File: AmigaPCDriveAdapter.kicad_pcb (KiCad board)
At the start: 2 copper layers, 99.1 x 30.5 mm, 19 parts, among them P1 CONN_01X04, P2 CONN_01X04, U1 74LS38

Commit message: Version Kicad 5 V2.0
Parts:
- removed LOGO: Symbol_OSHW-Logo_SilkScreen, Symbols:Symbol_OSHW-Logo_SilkScreen
- added OSHW: OSHW-Logo_5.7x6mm_SilkScreen, Symbol:OSHW-Logo_5.7x6mm_SilkScreen, F.Cu at (163.5, 118.5)
- C1, C4: footprint Capacitors_SMD:C_1206_HandSoldering -> Capacitor_Tantalum_SMD:CP_EIA-3216-12_Kemet-S
- C2: footprint Capacitors_SMD:C_1206_HandSoldering -> Capacitor_SMD:C_1206_3216Metric_Pad1.42x1.75mm_HandSolder
- C3: footprint Capacitors_SMD:C_1206_HandSoldering -> Capacitor_SMD:C_1206_3216Metric_Pad1.42x1.75mm_HandSolder; moved to B.Cu
- D1: footprint LEDs:LED_1206 -> LED_SMD:LED_1206_3216Metric_Pad1.42x1.75mm_HandSolder
- P1: footprint Pin_Headers:Pin_Header_Straight_1x04 -> Connector_PinHeader_2.54mm:PinHeader_1x04_P2.54mm_Vertical
- P2: footprint Pin_Headers:Pin_Header_Angled_1x04 -> Connector_PinHeader_2.54mm:PinHeader_1x04_P2.54mm_Horizontal
- R1, R2, R6, R8: footprint Resistors_SMD:R_1206_HandSoldering -> Resistor_SMD:R_1206_3216Metric_Pad1.42x1.75mm_HandSolder
- R3, R4, R5, R7: footprint Resistors_SMD:R_1206_HandSoldering -> Resistor_SMD:R_1206_3216Metric_Pad1.42x1.75mm_HandSolder; moved to B.Cu
- TO_FLOPPY1: footprint Socket_Strips:Socket_Strip_Straight_2x17 -> Connector_PinSocket_2.54mm:PinSocket_2x17_P2.54mm_Vertical
- U1: footprint Housings_DIP:DIP-14_W7.62mm -> Package_DIP:DIP-14_W7.62mm
- moved C3 58.1 mm to (164.2, 113.0)
- moved R7 51.2 mm to (145.6, 118.1), turned to 180 degrees
- moved R5 46.3 mm to (155.8, 118.1)
- moved C2 34.1 mm to (178.7, 103.5)
- moved R6 31.0 mm to (221.2, 111.1)
- moved R1 30.5 mm to (185.4, 104.8)
- moved R2 18.3 mm to (203.2, 111.1)
- moved R8 11.7 mm to (173.8, 109.2), turned to 0 degrees
- moved C4 10.9 mm to (164.5, 106.0), turned to 180 degrees
- moved U1 10.2 mm to (157.5, 114.3)
- moved R4 6.18 mm to (211.0, 109.9)
- moved TO_AMIGA1 5.08 mm to (172.7, 119.4)
- moved TO_FLOPPY1 2.54 mm to (180.3, 99.1), turned to 270 degrees
- moved C1 2.16 mm to (177.2, 98.4)
- moved R3 1.95 mm to (211.2, 104.8)
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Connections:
- TO_FLOPPY1 pad 2: (no net) -> Net-(TO_FLOPPY1-Pad2)
- U1 pad 10: (no net) -> Net-(U1-Pad10)
- U1 pad 11: (no net) -> Net-(U1-Pad11)
- U1 pad 12: (no net) -> Net-(U1-Pad12)
- U1 pad 13: (no net) -> Net-(U1-Pad13)
- U1 pad 8: (no net) -> Net-(U1-Pad8)
- U1 pad 9: (no net) -> Net-(U1-Pad9)
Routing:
- net +5V: track 161.3 -> 111.4 mm, vias 2 -> 1
- net Net-(R5-Pad1): track 47.0 -> 10.3 mm
- net ~REDWC: track 73.5 -> 108.2 mm, vias 2 -> 0
- net +12V: track 83.4 -> 50.0 mm
- net ~RDATA: track 52.5 -> 23.7 mm, vias 1 -> 0
- net ~INDEX: track 51.4 -> 32.7 mm, vias 1 -> 0
- net GND: track 184.9 -> 175.1 mm, vias 1 -> 0
- net ~MOTEA: track 44.2 -> 53.7 mm
- net ~TRK00: track 33.0 -> 25.0 mm
- net Net-(TO_AMIGA1-Pad4): track 19.0 -> 23.7 mm
- net Net-(TO_AMIGA1-Pad24): track 19.0 -> 23.7 mm
- net Net-(TO_AMIGA1-Pad18): track 19.0 -> 23.7 mm
- net Net-(TO_AMIGA1-Pad16): track 19.0 -> 23.7 mm
- net Net-(TO_AMIGA1-Pad22): track 19.0 -> 23.7 mm
- net Net-(TO_AMIGA1-Pad14): track 19.0 -> 23.7 mm
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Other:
- net class +12V: trace_width 0.35 -> 0.3
- net class +5V: trace_width 0.35 -> 0.3
- net class GND: trace_width 0.35 -> 0.3
- board text added: "+12V GND GND +5V"
- board text added: "RETROBITLAB RBL008.002"
- board text added: "designed by R.G.2018/2021"
- board text added: "in memoriam A.S. - G.D."
- board text removed: "R B B Y"
- board text removed: "RETROBITLAB RBL008.001"
- board text removed: "designed by R.G.2018/19"
- board text removed: "in memoriam A.S.-G.D."

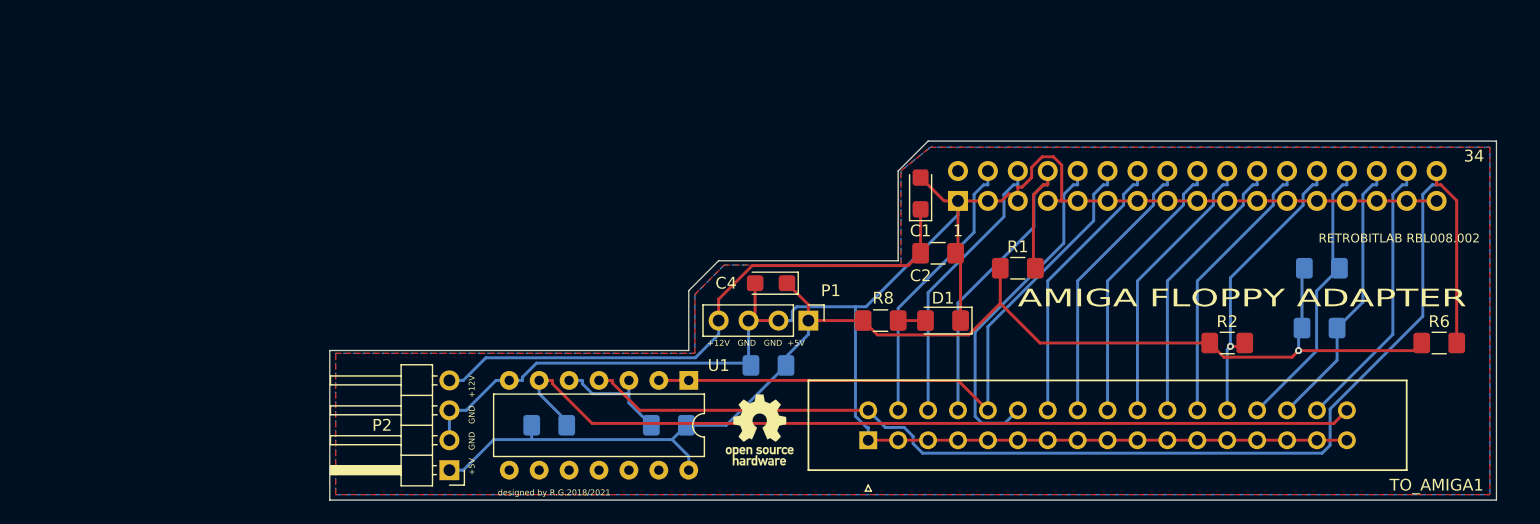
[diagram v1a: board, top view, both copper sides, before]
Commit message: Updated to drop the rescue file
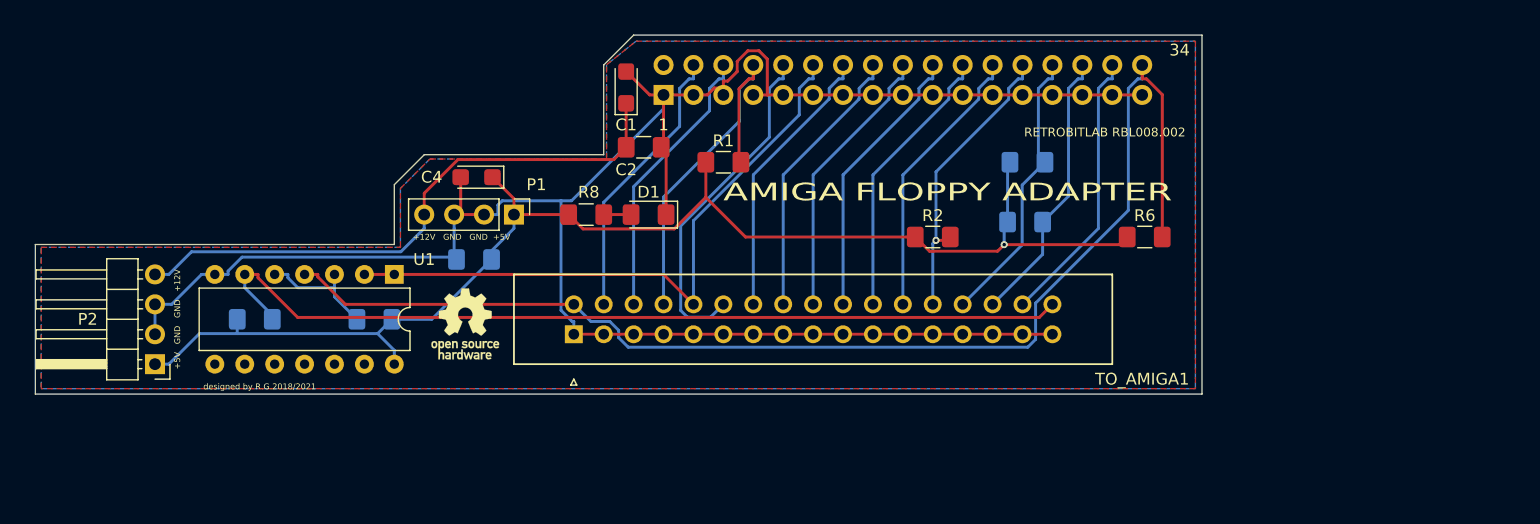
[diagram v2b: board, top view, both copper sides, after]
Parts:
- moved C1 26.6 mm to (152.2, 89.4)
- moved C2 26.6 mm to (153.7, 94.5)
- moved C3 26.6 mm to (139.2, 104.0)
- moved C4 26.6 mm to (139.5, 97.0)
- moved D1 26.6 mm to (154.1, 100.2)
- moved OSHW 26.6 mm to (138.5, 109.5)
- moved P1 26.6 mm to (142.6, 100.2)
- moved P2 26.6 mm to (112.2, 112.9)
- moved R1 26.6 mm to (160.4, 95.8)
- moved R2 26.6 mm to (178.2, 102.1)
- moved R3 26.6 mm to (186.2, 95.8)
- moved R4 26.6 mm to (186.0, 100.9)
- moved R5 26.6 mm to (130.8, 109.1)
- moved R6 26.6 mm to (196.2, 102.1)
- moved R7 26.6 mm to (120.6, 109.1)
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
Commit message: Generated with latest version of KiCAD 5.1.9
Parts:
- removed OSHW: OSHW-Logo_5.7x6mm_SilkScreen, Symbol:OSHW-Logo_5.7x6mm_SilkScreen
- C2, C3: footprint Capacitor_SMD:C_1206_3216Metric_Pad1.42x1.75mm_HandSolder -> Capacitor_SMD:C_1206_3216Metric_Pad1.33x1.80mm_HandSolder
- R1, R2, R3, R4, R5, R6, R7, R8: footprint Resistor_SMD:R_1206_3216Metric_Pad1.42x1.75mm_HandSolder -> Resistor_SMD:R_1206_3216Metric_Pad1.30x1.75mm_HandSolder
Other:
- outline, holes or cut-outs redrawn
- board text added: "designed by R.G.2018/2021/2022"
- board text removed: "designed by R.G.2018/2021"
